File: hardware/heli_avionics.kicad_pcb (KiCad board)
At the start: 4 copper layers, 65.5 x 39 mm, 73 parts, among them J1 Pin_Header_2x3, J10 Pin_Header_1x1, J2 JST_PH_01x02, J3 JST_XH_01x02, J4 JST_XH_01x02, J5 JST_PH_01x03, J6 Conn_01x01, J7 JST_ZH_01x02, J8 Conn_01x01, J9 Pin_Header_1x2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

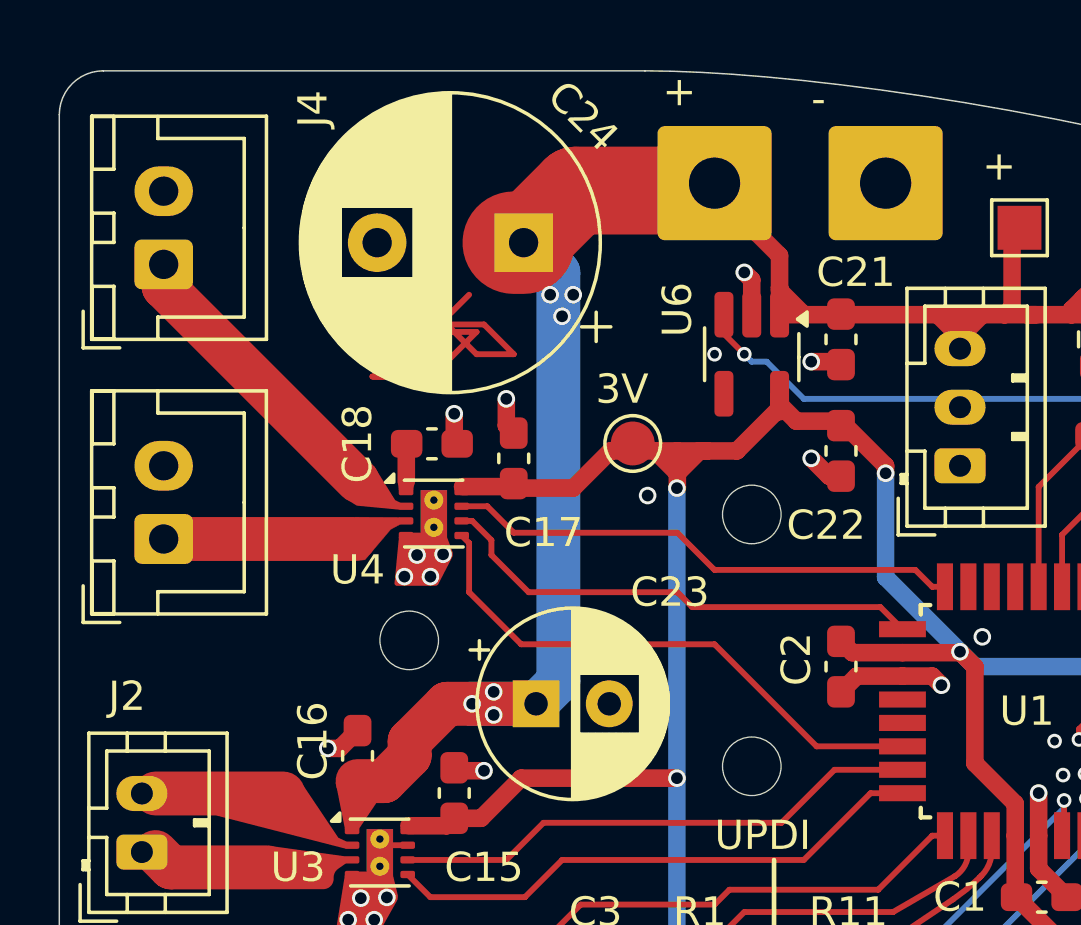
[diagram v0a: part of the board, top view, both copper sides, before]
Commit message: Experiment to see if 3rd motor driver is possible
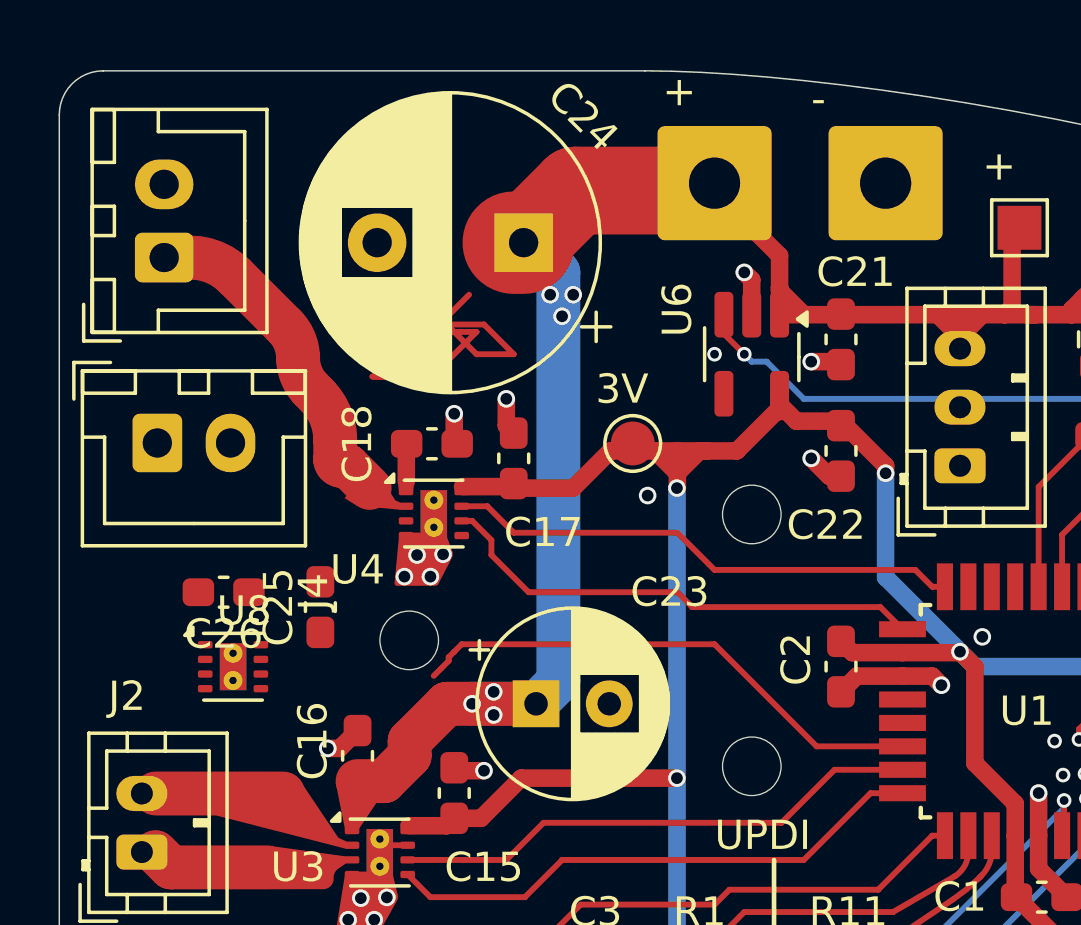
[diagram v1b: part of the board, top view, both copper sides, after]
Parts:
- added C25: 22uF, Capacitor_SMD:C_0603_1608Metric_Pad1.08x0.95mm_HandSolder, F.Cu at (109.0, 118.4)
- added C26: 22uF, Capacitor_SMD:C_0603_1608Metric_Pad1.08x0.95mm_HandSolder, F.Cu at (105.7, 117.9)
- added U8: DRV8212, heli-footprints:WSON-8-1EP_2x2mm_P0.5mm_EP0.9x1.6mm_ThermalVias, F.Cu at (106.0, 120.4)
- moved J3 9.61 mm to (103.6, 106.4)
- moved J4 6.10 mm to (103.4, 112.8), turned to 0 degrees
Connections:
- U2 pad 21: GND -> (no net)
- U4 pad 2: Net-(J4-Pin_1) -> Net-(J3-Pin_1)
- U4 pad 5: /PF2 -> /PD7
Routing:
- net Net-(J4-Pin_1): track 10.1 -> 0.00 mm
- net Net-(J3-Pin_1): track 6.50 -> 11.6 mm
- net /PF2: track 19.0 -> 18.0 mm

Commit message: Correct pin ordering for 3rd motor driver
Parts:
- J7: value JST_ZH_01x02 -> JST_1.25mm
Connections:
- U1 pad 21: unconnected-(U1-PF1/TOSC2-Pad21) -> /PF1
- U8 pad 7: /PD6 -> /PF1
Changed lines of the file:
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@@
 	(net 15 "Net-(Q1-D)")
 	(net 16 "Net-(R2-Pad1)")
-	(net 17 "unconnected-(U1-PF1{slash}TOSC2-Pad21)")
+	(net 17 "/PF1")
 	(net 18 "/PD7")
 	(net 19 "/PF4")
@@
 		)
 		(property "Value" "JST_XH_01x02"
-			(at 1.25 4.6 360)
+			(at 1.25 4.6 0)
 			(layer "F.Fab")
 			(effects
@@
 		(tags "capacitor handsolder")
 		(property "Reference" "C26"
-			(at 0 -1.43 360)
+			(at 0 -1.43 0)
 			(layer "F.SilkS")
 			(effects
@@
 		)
 		(property "Value" "22uF"
-			(at 0 1.43 360)
+			(at 0 1.43 0)
 			(layer "F.Fab")
 			(effects
@@
 			)
 		)
-		(property "Value" "JST_ZH_01x02"
+		(property "Value" "JST_1.25mm"
 			(at 0.62 2.35 180)
 			(layer "F.Fab")
@@
 			(size 1.6 0.55)
 			(layers "F.Cu" "F.Paste" "F.Mask")
-			(net 17 "unconnected-(U1-PF1{slash}TOSC2-Pad21)")
+			(net 17 "/PF1")
 			(pinfunction "PF1/TOSC2")
-			(pintype "bidirectional+no_connect")
+			(pintype "bidirectional")
 			(teardrops
 				(best_length_ratio 0.5)
@@
 			(roundrect_rratio 0.25)
 			(net 9 "Net-(J3-Pin_1)")
-			(pinfunction "OUT2")
-			(pintype "output")
+			(pinfunction "OUT1")
+			(pintype "passive")
 		)
 		(pad "4" smd roundrect
@@
 			(roundrect_rratio 0.25)
 			(net 10 "Net-(J4-Pin_1)")
-			(pinfunction "OUT2")
-			(pintype "output")
+			(pinfunction "OUT1")
+			(pintype "passive")
 		)
 		(pad "4" smd roundrect
@@
 			(layers "F.Cu" "F.Paste" "F.Mask")
 			(roundrect_rratio 0.25)
-			(net 29 "/PD6")
+			(net 17 "/PF1")
 			(pinfunction "MODE")
 			(pintype "input")

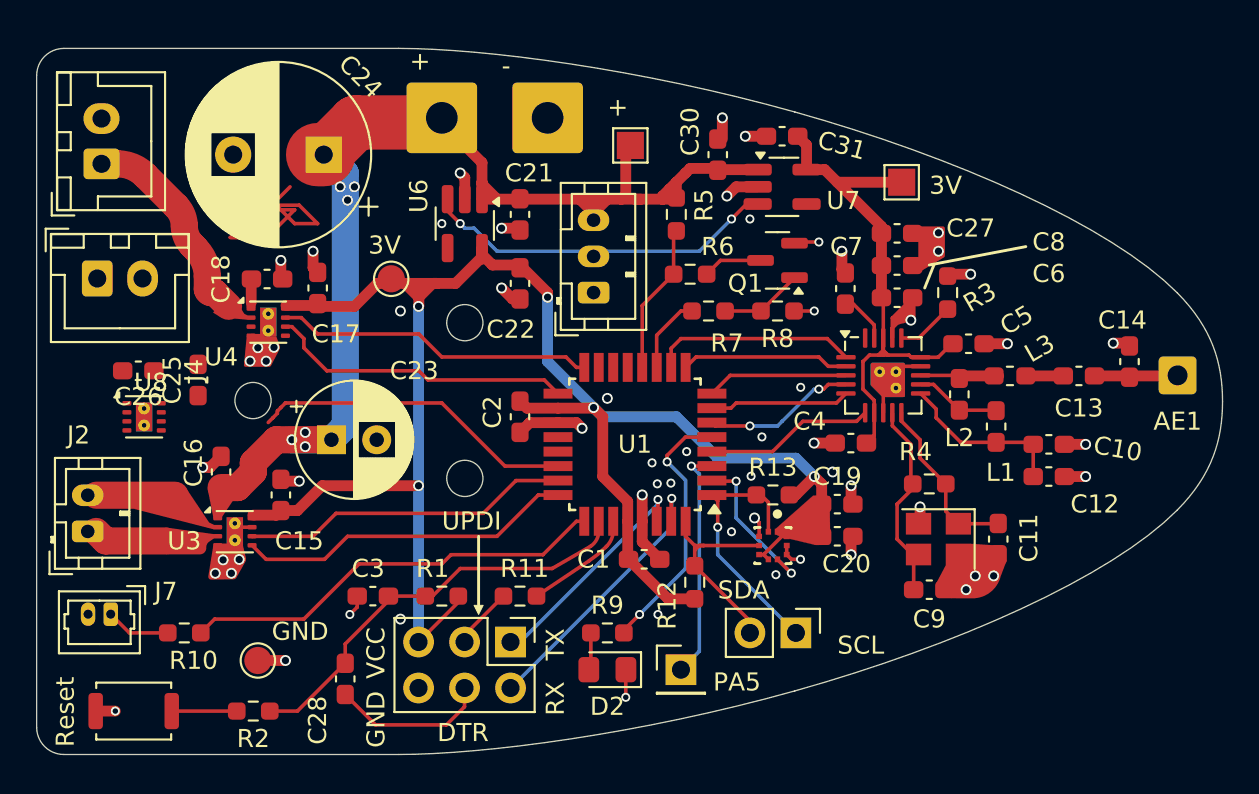
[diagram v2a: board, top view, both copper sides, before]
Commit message: Almost done with new motor driver layout
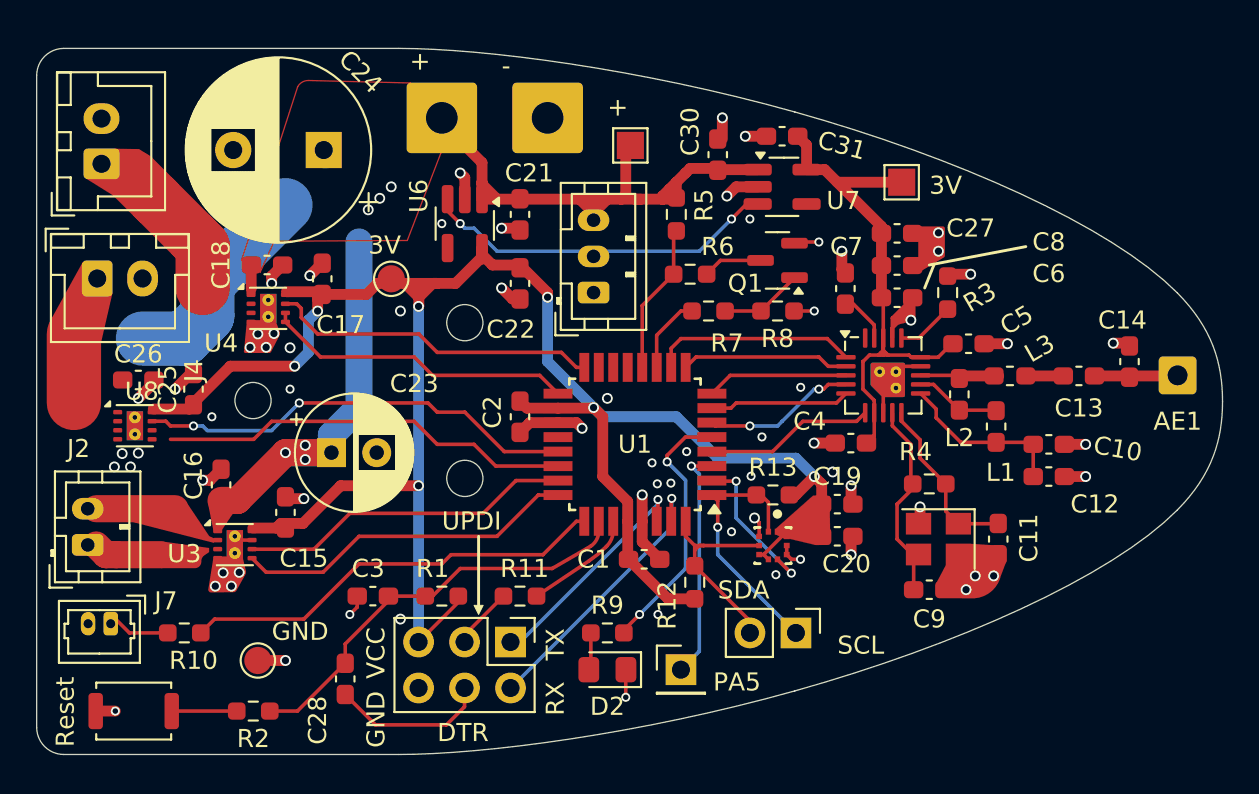
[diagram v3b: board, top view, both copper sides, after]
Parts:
- moved C15 1.00 mm to (113.8, 125.7)
- moved C18 0.77 mm to (112.8, 112.0)
- moved U4 0.76 mm to (112.8, 114.4)
- moved J2 0.75 mm to (102.9, 127.5)
- moved C23 0.71 mm to (116.3, 122.4)
- moved U3 0.71 mm to (111.0, 127.5)
- moved C16 0.71 mm to (110.2, 124.2)
- moved U8 0.71 mm to (105.5, 120.9)
- moved C17 0.57 mm to (115.8, 112.8)
- moved C25 0.57 mm to (108.7, 118.9)
- moved J7 0.53 mm to (104.1, 131.8)
- moved C26 0.51 mm to (105.7, 118.4), turned to 0 degrees
- moved C24 0.25 mm to (115.9, 105.7)
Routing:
- net +BATT: track 87.0 -> 54.9 mm
- net /PF1: track 0.00 -> 24.4 mm, vias 0 -> 2
- net VCC: track 100.5 -> 113.5 mm, vias 5 -> 7
- net (no net): track 0.00 -> 12.0 mm
- net /PF2: track 18.0 -> 22.8 mm
- net Net-(J3-Pin_1): track 11.6 -> 7.67 mm
- net Net-(J4-Pin_1): track 0.00 -> 3.81 mm
- net GND: track 54.4 -> 56.8 mm, vias 61 -> 70
- net /PD6: track 17.6 -> 18.3 mm

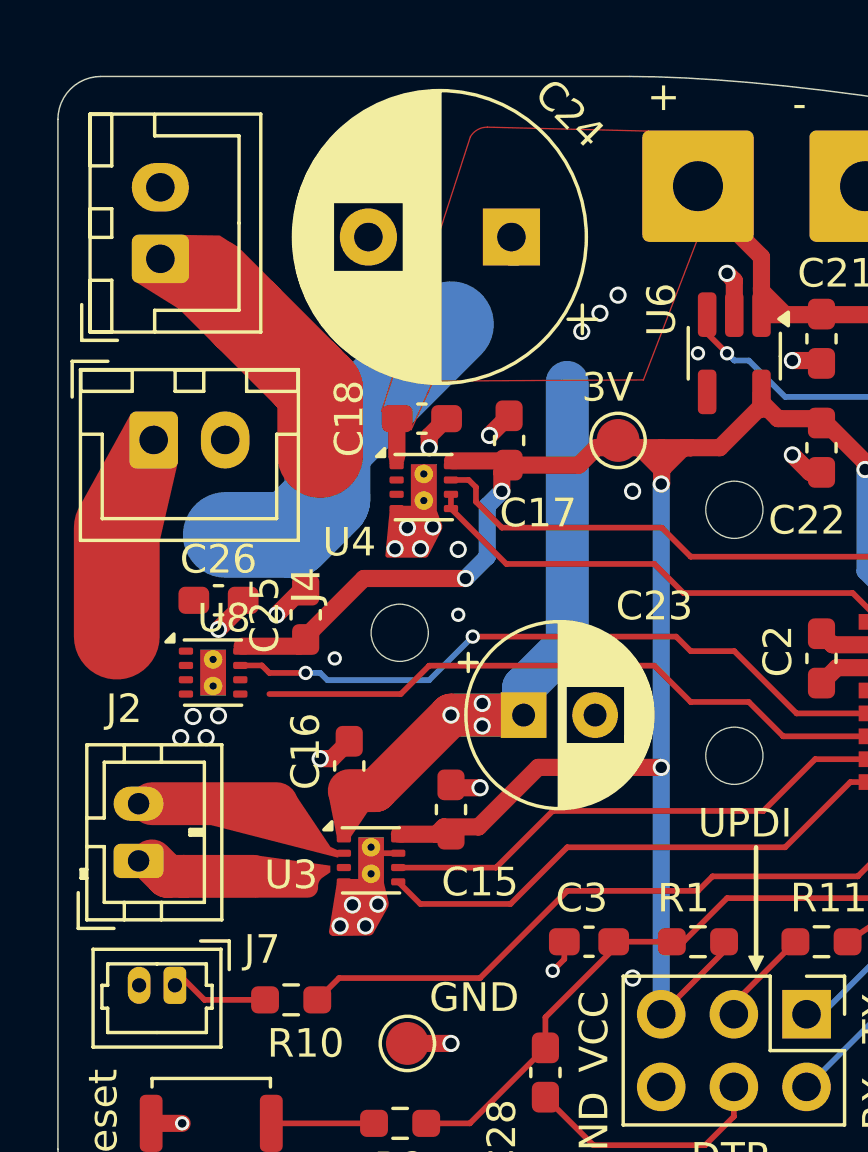
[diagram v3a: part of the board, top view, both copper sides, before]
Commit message: Finished routing for 3rd motor driver
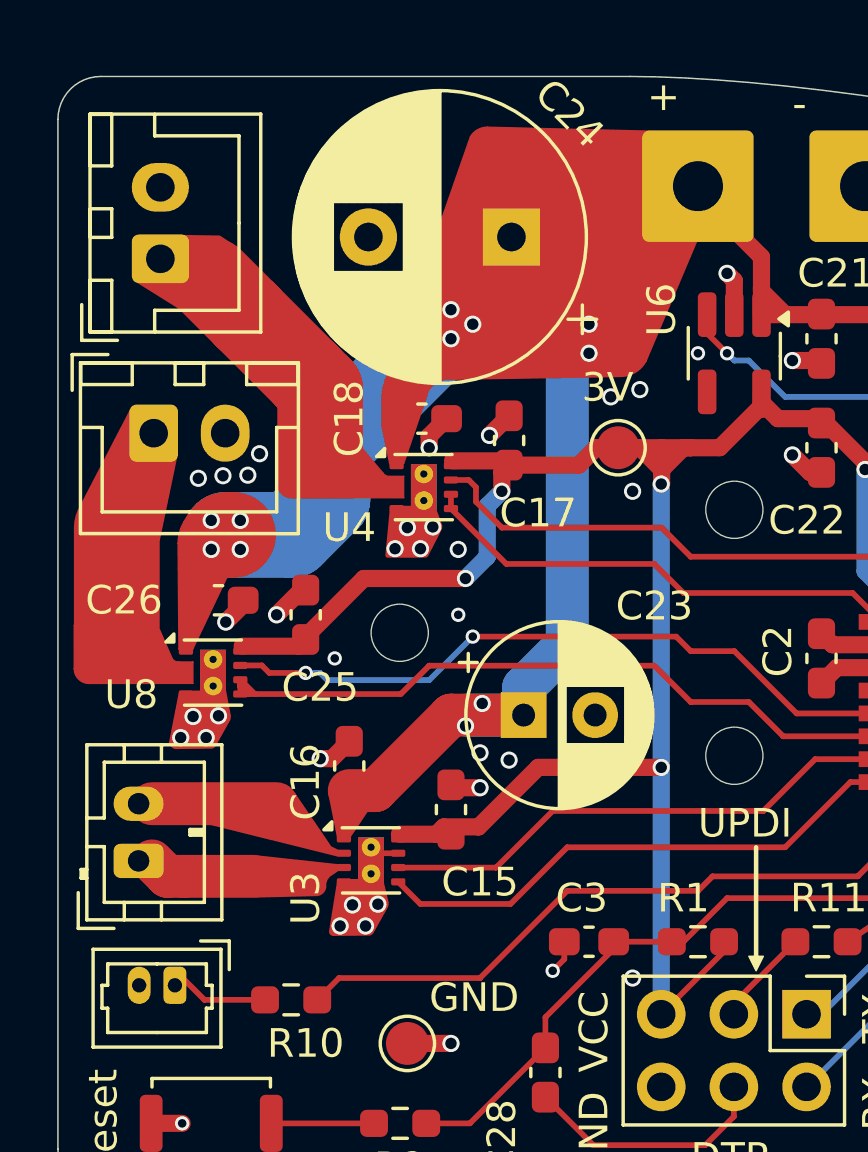
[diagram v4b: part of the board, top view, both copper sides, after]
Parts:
- moved TP2 0.25 mm to (119.6, 113.0)
- moved J4 0.24 mm to (103.4, 112.5)
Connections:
- U2 pad 21: (no net) -> GND
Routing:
- net +BATT: track 54.9 -> 67.5 mm, vias 6 -> 12
- net (no net): track 12.0 -> 0.00 mm
- net /PF2: track 22.8 -> 25.7 mm
- net GND: track 56.8 -> 56.4 mm, vias 70 -> 82

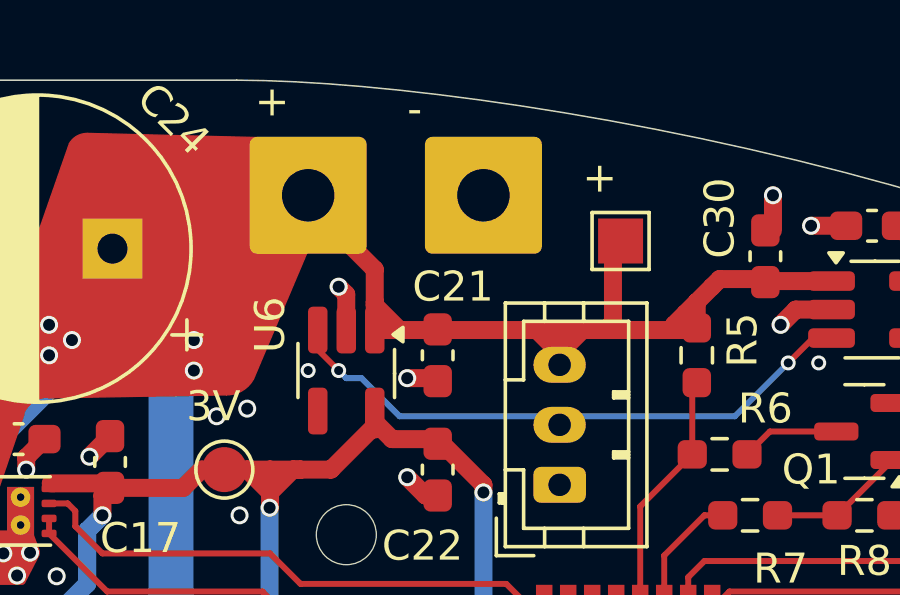
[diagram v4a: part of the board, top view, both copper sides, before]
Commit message: Increased trace width to handle battery charging current
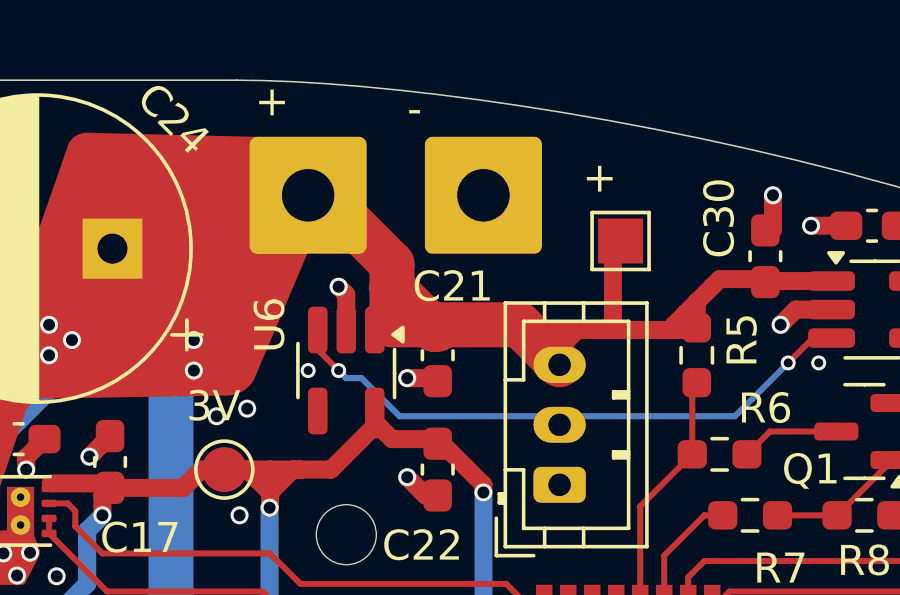
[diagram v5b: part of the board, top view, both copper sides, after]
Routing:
- net +BATT: track 67.5 -> 68.3 mm
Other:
- board text added: "Thicker trace for (reverse) charging current"
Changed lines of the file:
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@@
+		)
+	)
+	(gr_text "Thicker trace for\n(reverse) charging current"
+		(at 123.698 111.76 0)
+		(layer "Cmts.User")
+		(effects
+			(font
+				(size 1 1)
+				(thickness 0.15)
+			)
+			(justify left bottom)
 		)
 	)
@@
 	)
 	(segment
+		(start 123.444 104.394)
+		(end 125.222 106.172)
+		(width 1.5)
+		(layer "F.Cu")
+		(net 12)
+	)
+	(segment
+		(start 125.222 106.172)
+		(end 125.222 106.934)
+		(width 1.5)
+		(layer "F.Cu")
+		(net 12)
+	)
+	(segment
 		(start 113.792 122.37775)
 		(end 111.1515 125.01825)
@@
 	)
 	(segment
-		(start 124.648 107.55)
-		(end 125.476 108.378)
-		(width 0.6)
-		(layer "F.Cu")
-		(net 12)
-	)
-	(segment
 		(start 135.001 107.823)
 		(end 135.382 107.442)
@@
 	)
 	(segment
-		(start 124.648 108.378)
-		(end 125.476 108.378)
-		(width 0.6)
-		(layer "F.Cu")
-		(net 12)
-	)
-	(segment
-		(start 130.81 108.378)
-		(end 131.572 108.378)
-		(width 0.6)
+		(start 123.444 103.886)
+		(end 123.444 104.394)
+		(width 1.5)
+		(layer "F.Cu")
+		(net 12)
+	)
+	(segment
+		(start 126.746 108.3575)
+		(end 126.6455 108.3575)
+		(width 1.5)
 		(layer "F.Cu")
 		(net 12)
@@
 	)
 	(segment
-		(start 130.81 109.538)
-		(end 130.81 109.14)
-		(width 0.6)
-		(layer "F.Cu")
-		(net 12)
-	)
-	(segment
 		(start 133.096 108.378)
 		(end 133.42 108.378)
@@
 	)
 	(segment
-		(start 124.648 106.36)
-		(end 124.648 107.442)
+		(start 131.572 108.378)
+		(end 129.65 108.378)
+		(width 0.6)
+		(layer "F.Cu")
+		(net 12)
+	)
+	(segment
+		(start 129.476 108.204)
+		(end 130.524 109.252)
+		(width 1.5)
+		(layer "F.Cu")
+		(net 12)
+	)
+	(segment
+		(start 126.6455 108.3575)
+		(end 125.222 106.934)
+		(width 1.5)
+		(layer "F.Cu")
+		(net 12)
+	)
+	(segment
+		(start 131.572 108.378)
+		(end 131.398 108.378)
 		(width 0.6)
 		(layer "F.Cu")
@@
 	)
 	(segment
+		(start 130.524 109.252)
+		(end 130.81 109.538)
+		(width 1.5)
+		(layer "F.Cu")
+		(net 12)
+	)
+	(segment
 		(start 134.62 108.378)
 		(end 135.4525 108.378)
@@
 		(start 135.382 108.3075)
 		(end 135.382 107.442)
-		(width 0.6)
-		(layer "F.Cu")
-		(net 12)
-	)
-	(segment
-		(start 130.048 108.378)
-		(end 130.81 108.378)
 		(width 0.6)
 		(layer "F.Cu")
@@
 	)
 	(segment
-		(start 130.81 109.538)
-		(end 130.81 108.378)
-		(width 0.6)
-		(layer "F.Cu")
-		(net 12)
-	)
-	(segment
 		(start 137.9565 106.746)
 		(end 137.922 106.7805)
@@
 	)
 	(segment
-		(start 131.572 108.378)
-		(end 132.334 108.378)
-		(width 0.6)
-		(layer "F.Cu")
-		(net 12)
-	)
-	(segment
-		(start 124.648 107.442)
-		(end 124.648 107.55)
+		(start 129.65 108.378)
+		(end 129.476 108.204)
+		(width 0.6)
+		(layer "F.Cu")
+		(net 12)
+	)
+	(segment
+		(start 131.398 108.378)
+		(end 130.524 109.252)
 		(width 0.6)
 		(layer "F.Cu")
@@
 	)
 	(segment
-		(start 130.81 109.14)
-		(end 131.572 108.378)
-		(width 0.6)
-		(layer "F.Cu")
-		(net 12)
-	)
-	(segment
-		(start 130.81 109.14)
-		(end 130.048 108.378)
-		(width 0.6)
-		(layer "F.Cu")
-		(net 12)
-	)
-	(segment
 		(start 132.842 105.41)
 		(end 132.588 105.664)
@@
 	)
 	(segment
-		(start 122.428 104.14)
-		(end 124.648 106.36)
+		(start 125.222 106.934)
+		(end 125.222 108.204)
+		(width 1.5)
+		(layer "F.Cu")
+		(net 12)
+	)
+	(segment
+		(start 125.222 108.204)
+		(end 129.476 108.204)
+		(width 1.5)
+		(layer "F.Cu")
+		(net 12)
+	)
+	(segment
+		(start 132.334 108.378)
+		(end 131.572 108.378)
 		(width 0.6)
 		(layer "F.Cu")
@@
 		(start 137.8215 106.68)
 		(end 137.922 106.7805)
-		(width 0.6)
-		(layer "F.Cu")
-		(net 12)
-	)
-	(segment
-		(start 124.648 107.442)
-		(end 124.648 108.378)
 		(width 0.6)
 		(layer "F.Cu")
@@
 	)
 	(segment
-		(start 125.476 108.378)
-		(end 130.048 108.378)
-		(width 0.6)
-		(layer "F.Cu")
-		(net 12)
+		(start 122.428 103.886)
+		(end 123.444 103.886)
+		(width 1.5)
+		(layer "F.Cu")
+		(net 12)
